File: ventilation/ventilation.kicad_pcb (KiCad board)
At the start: 2 copper layers, 36.8 x 27 mm, 34 parts, among them J1 Conn_01x03_Pin, J2 Conn_01x04_Pin, J3 Conn_01x04_Pin, J7 Conn_01x02_Pin, Q1 IRLML6402, Q2 BC847, U1 STM32L051C8Tx, U2 MCP1700x-330xxTT

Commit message: New version
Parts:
- added H1: MountingHole, MountingHole:MountingHole_2.5mm, F.Cu at (191.4, 79.2)
- added H2: MountingHole, MountingHole:MountingHole_2.5mm, F.Cu at (191.4, 97.8)
- moved NRF1 8.91 mm to (183.9, 84.1), turned to 0 degrees
- moved C8 7.23 mm to (184.0, 84.9), turned to -90 degrees
- moved C7 5.85 mm to (186.6, 84.9), turned to -90 degrees
- moved R7 5.56 mm to (172.4, 100.0)
- moved C4 5.35 mm to (176.1, 91.2)
- moved C10 5.20 mm to (167.8, 87.3), turned to 90 degrees
- moved R9 4.63 mm to (166.0, 78.1), turned to -90 degrees
- moved C5 4.15 mm to (181.4, 84.9)
- moved C2 3.67 mm to (174.4, 84.9), turned to -90 degrees
- moved R3 3.64 mm to (168.8, 95.8), turned to 180 degrees
- moved R6 3.28 mm to (178.8, 98.2), turned to 180 degrees
- moved R10 2.77 mm to (166.7, 81.3), turned to 0 degrees
- moved C6 2.72 mm to (172.3, 97.8), turned to 0 degrees
- moved C9 2.57 mm to (177.7, 97.9), turned to 180 degrees
- moved R8 2.57 mm to (177.7, 100.1), turned to 180 degrees
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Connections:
- J1 pad 2: /VCC_SERVO -> /SIG_SERVO
- J1 pad 3: /SIG_SERVO -> /VCC_SERVO
- J2 pad 3: /I2C_SDA -> /I2C_SCL
- J2 pad 4: /I2C_SCL -> /I2C_SDA
- U1 pad 12: unconnected-(U1-PA2-Pad12) -> /SW_SERVO
- U1 pad 13: /SPI_CE -> unconnected-(U1-PA3-Pad13)
- U1 pad 14: /SPI_CSN -> unconnected-(U1-PA4-Pad14)
- U1 pad 21: unconnected-(U1-PB10-Pad21) -> /SPI_CSN
- U1 pad 22: unconnected-(U1-PB11-Pad22) -> /SPI_CE
- U1 pad 25: /LED_GREEN -> /LED_RED
- U1 pad 28: /LED_RED -> /LED_GREEN
- U1 pad 6: /SW_SERVO -> unconnected-(U1-PH1-Pad6)
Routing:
- net +3V3: track 0.00 -> 90.0 mm, vias 0 -> 6
- net GND: track 0.00 -> 37.8 mm, vias 0 -> 5
- net /RESET: track 0.00 -> 31.2 mm, vias 0 -> 1
- net /BOOT: track 0.00 -> 27.6 mm
- net +BATT: track 0.00 -> 18.0 mm
- net /I2C_SCL: track 0.00 -> 16.2 mm
- net /I2C_SDA: track 0.00 -> 14.9 mm
- net /SPI_SCK: track 0.00 -> 13.1 mm
- net /G_FET: track 0.00 -> 12.7 mm
- net /VCC_SERVO: track 0.00 -> 12.2 mm
- net /ADC_V_EXT: track 0.00 -> 12.1 mm
- net Net-(U1-PB3): track 0.00 -> 10.9 mm
- net /SWCLK: track 0.00 -> 9.44 mm
- net /LED_GREEN: track 0.00 -> 9.02 mm
- net /USART1_TX: track 0.00 -> 7.75 mm
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- added copper zone on B.Cu, net GND
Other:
- board size 36.8 x 27 mm -> 38 x 27 mm

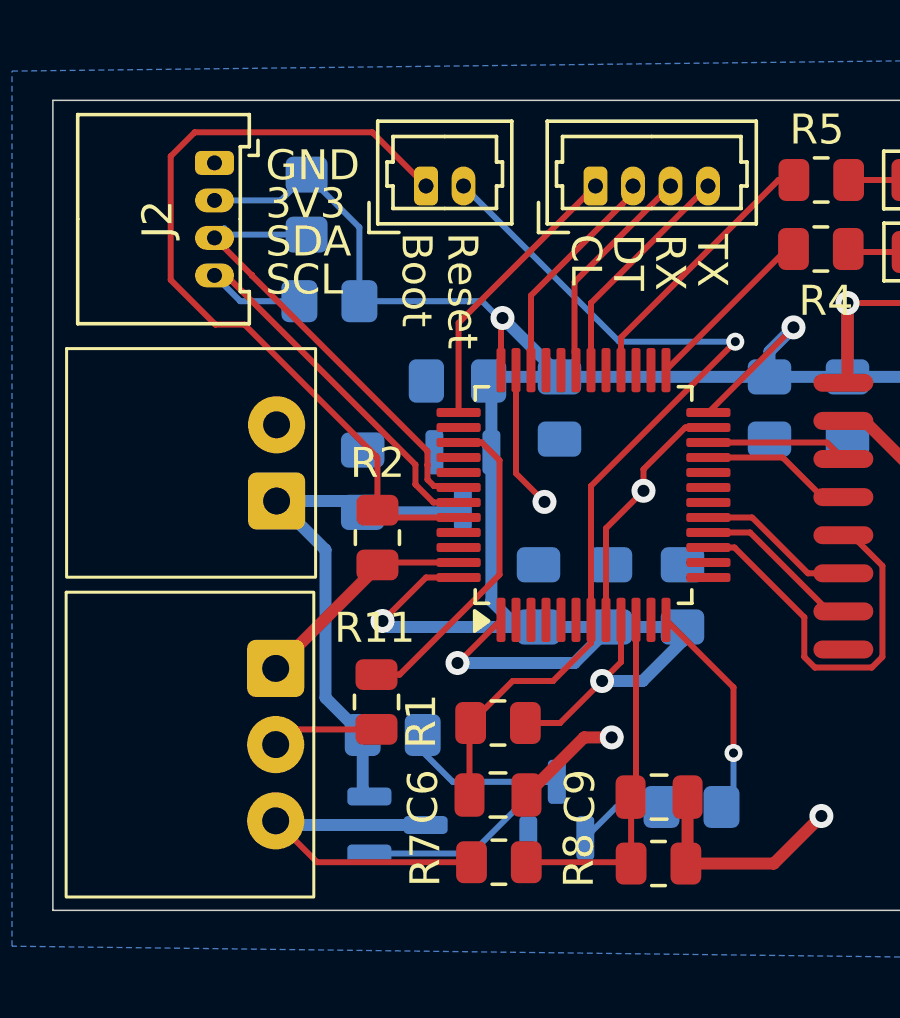
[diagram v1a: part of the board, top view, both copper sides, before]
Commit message: Changed SOT23 footprints to hand solder
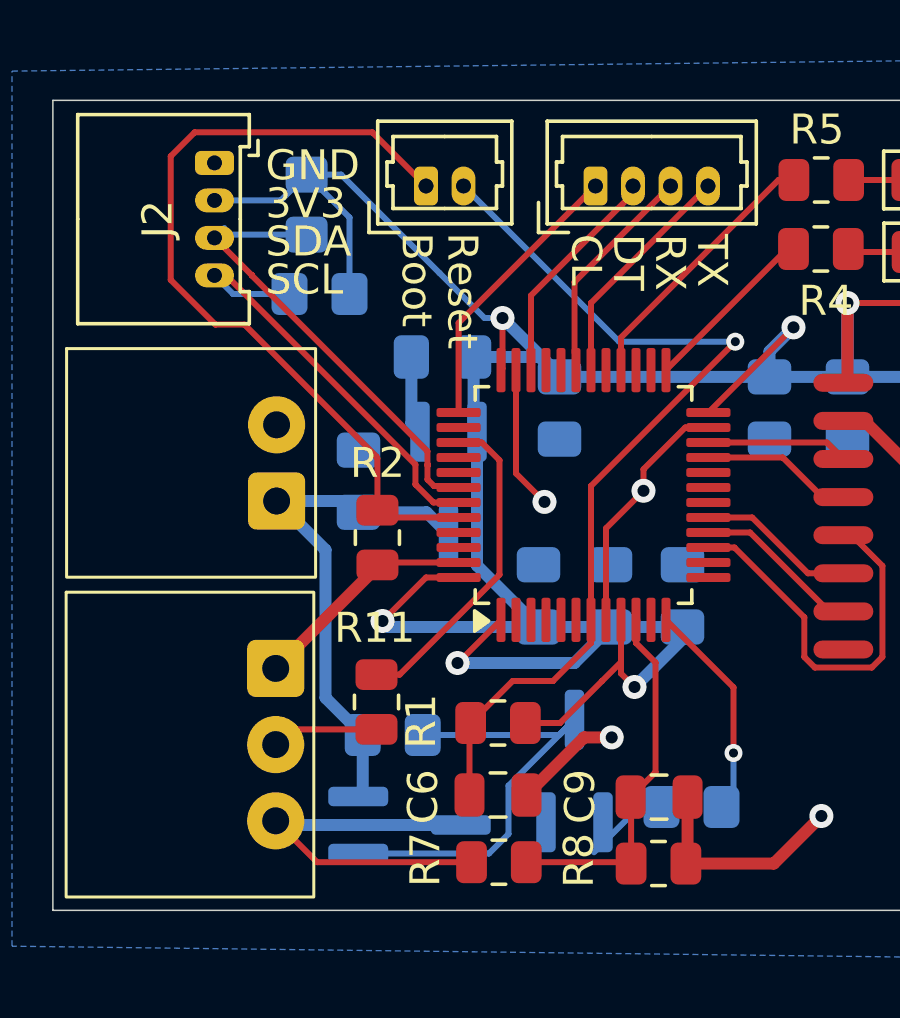
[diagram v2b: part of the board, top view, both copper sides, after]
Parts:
- Q1, Q2, U2: footprint Package_TO_SOT_SMD:SOT-23 -> Package_TO_SOT_SMD:TSOT-23_HandSoldering
- moved Q2 1.43 mm to (174.9, 97.0)
- moved C11 0.94 mm to (170.5, 83.2)
- moved U2 0.49 mm to (170.7, 87.4)
- moved R10 0.41 mm to (166.4, 81.1)
- moved Q1 0.40 mm to (169.4, 98.8)
- moved C10 0.14 mm to (167.7, 87.3)
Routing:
- net +3V3: track 90.0 -> 96.5 mm
- net /G_FET: track 12.7 -> 15.8 mm
- net GND: track 37.8 -> 40.4 mm
- net /VCC_SERVO: track 12.2 -> 13.3 mm

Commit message: New version
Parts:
- added J4: Conn_01x04_Pin, PVDW_custom:Molex_PicoBlade_1x04_P1.25mm_Vertical, F.Cu at (185.7, 98.2)
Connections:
- U1 pad 13: unconnected-(U1-PA3-Pad13) -> /PA3
- U1 pad 14: unconnected-(U1-PA4-Pad14) -> /PA4
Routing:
- net /PA4: track 0.00 -> 11.3 mm
- net /PA3: track 0.00 -> 9.79 mm
- net +3V3: track 96.5 -> 104.5 mm
- net GND: track 40.4 -> 39.3 mm, vias 5 -> 4

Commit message: New version
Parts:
- removed C5: 100n, Capacitor_SMD:C_0805_2012Metric_Pad1.18x1.45mm_HandSolder
- removed J1: Conn_01x03_Pin, PVDW_custom:Connector_1x3_p2.54_hortizontal
- removed J4: Conn_01x04_Pin, PVDW_custom:Molex_PicoBlade_1x04_P1.25mm_Vertical
- removed J5: ~, PVDW_custom:Connector_1x2_p2.54_horizontal
- removed J7: Conn_01x02_Pin, PVDW_custom:Molex_PicoBlade_P1.25mm_Vertical
- added J6: Conn_01x10_Pin, PVDW_custom:FFC_1x10_P1.00mm_Horizontal, F.Cu at (177.2, 80.1)
- J2: footprint PVDW_custom:Molex_PicoBlade_53048-0410_1x04_P1.25mm_Horizontal -> PVDW_custom:Connector_1x4_p2.54_hortizontal
- J3: footprint PVDW_custom:Molex_PicoBlade_1x04_P1.25mm_Vertical -> PVDW_custom:Connector_1x4_p2.54_hortizontal
- moved J3 23.6 mm to (164.8, 98.5)
- moved R4 20.5 mm to (182.0, 100.0)
- moved D2 20.4 mm to (186.8, 97.7)
- moved R5 20.4 mm to (182.0, 97.7)
- moved D1 20.4 mm to (186.8, 100.1)
- moved R11 10.0 mm to (167.7, 84.7), turned to -90 degrees
- moved J2 8.97 mm to (164.8, 85.5), turned to 0 degrees
- moved C4 7.26 mm to (179.4, 84.7), turned to -90 degrees
- moved R9 6.56 mm to (172.3, 76.5), turned to 180 degrees
- moved R10 6.40 mm to (172.3, 78.7)
- moved C10 5.46 mm to (168.3, 92.8)
- moved R6 4.81 mm to (177.8, 93.5)
- moved C3 4.62 mm to (177.8, 89.1), turned to 0 degrees
- moved R1 4.57 mm to (168.0, 96.8), turned to -90 degrees
- moved R3 4.24 mm to (172.4, 93.5), turned to 0 degrees
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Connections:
- J3 pad 1: /SWCLK -> GND
- J3 pad 2: /SWDIO -> +BATT
- J3 pad 3: /USART1_RX -> /SIG_SERVO
- J3 pad 4: /USART1_TX -> /VCC_SERVO
- U1 pad 11: unconnected-(U1-PA1-Pad11) -> /LED_RED
- U1 pad 12: /SW_SERVO -> /LED_GREEN
- U1 pad 13: /PA3 -> /SW_SERVO
- U1 pad 14: /PA4 -> unconnected-(U1-PA4-Pad14)
- U1 pad 25: /LED_RED -> unconnected-(U1-PB12-Pad25)
- U1 pad 27: unconnected-(U1-PB14-Pad27) -> /PB14
- U1 pad 28: /LED_GREEN -> /PB15
- U1 pad 42: /I2C_SCL -> unconnected-(U1-PB6-Pad42)
- U1 pad 43: /I2C_SDA -> unconnected-(U1-PB7-Pad43)
- U1 pad 45: unconnected-(U1-PB8-Pad45) -> /I2C_SCL
- U1 pad 46: unconnected-(U1-PB9-Pad46) -> /I2C_SDA
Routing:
- net /SIG_SERVO: track 3.57 -> 19.5 mm, vias 0 -> 1
- net /PA4: track 11.3 -> 0.00 mm
- net GND: track 39.3 -> 29.4 mm, vias 4 -> 8
- net /PA3: track 9.79 -> 0.00 mm
- net /BOOT: track 27.6 -> 19.0 mm
- net /RESET: track 31.2 -> 38.0 mm, vias 1 -> 0
- net Net-(U1-PB3): track 10.9 -> 4.35 mm
- net /I2C_SCL: track 16.2 -> 21.8 mm
- net /I2C_SDA: track 14.6 -> 20.1 mm
- net /PB14: track 0.00 -> 5.30 mm
- net /PB15: track 0.00 -> 5.10 mm
- net /G_FET: track 15.8 -> 11.0 mm
- net /LED_GREEN: track 9.02 -> 5.41 mm
- net +3V3: track 104.5 -> 107.6 mm
- net /SW_SERVO: track 7.34 -> 4.52 mm
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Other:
- board size 38 x 27 mm -> 38 x 28.7 mm

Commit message: New versions
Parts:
- removed J6: Conn_01x10_Pin, PVDW_custom:FFC_1x10_P1.00mm_Horizontal
- added J1: Conn_01x10_Pin, Connector_PinHeader_2.54mm:PinHeader_2x05_P2.54mm_Vertical, F.Cu at (186.8, 75.9)
- Q1, Q2, U2: footprint Package_TO_SOT_SMD:TSOT-23_HandSoldering -> Package_TO_SOT_SMD:SOT-23
- moved R9 4.37 mm to (168.9, 79.2)
- moved R10 3.83 mm to (168.9, 77.0)
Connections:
- J2 pad 1: GND -> +3V3
- J2 pad 2: +3V3 -> GND
- J2 pad 3: /I2C_SCL -> /I2C_SDA
- J2 pad 4: /I2C_SDA -> /I2C_SCL
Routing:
- net /PB15: track 5.10 -> 13.2 mm
- net /USART1_RX: track 4.89 -> 12.3 mm
- net /SWCLK: track 8.22 -> 15.4 mm
- net /RESET: track 38.0 -> 44.8 mm
- net /PB14: track 5.30 -> 10.3 mm
- net /USART1_TX: track 5.10 -> 9.71 mm
- net /SWDIO: track 5.10 -> 9.01 mm
- net /BOOT: track 19.0 -> 22.6 mm
- net /I2C_SCL: track 21.8 -> 18.2 mm
- net GND: track 29.4 -> 26.3 mm, vias 8 -> 7
- net /G_FET: track 11.0 -> 13.8 mm, vias 0 -> 2
- net +3V3: track 107.6 -> 105.7 mm
- net /I2C_SDA: track 20.1 -> 21.4 mm

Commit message: Order versions
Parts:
- removed J1: Conn_01x10_Pin, Connector_PinHeader_2.54mm:PinHeader_2x05_P2.54mm_Vertical
- added Boot1: TestPoint, TestPoint:TestPoint_Pad_2.0x2.0mm, F.Cu at (167.8, 86.1)
- added J4: Conn_01x08_Pin, Connector_PinHeader_2.54mm:PinHeader_2x04_P2.54mm_Vertical, F.Cu at (176.0, 78.4)
- added Reset1: TestPoint, TestPoint:TestPoint_Pad_2.0x2.0mm, F.Cu at (168.6, 96.4)
- moved R1 4.41 mm to (172.4, 96.3), turned to 180 degrees
- moved R11 2.71 mm to (168.5, 82.1), turned to 0 degrees
- moved C6 0.67 mm to (172.4, 98.3)
- moved R2 0.54 mm to (168.2, 88.6), turned to 180 degrees
- moved R7 0.36 mm to (172.4, 100.4)
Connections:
- net Net-(U1-PB3) renamed /SIG_SERVO_OUT
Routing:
- net /RESET: track 44.8 -> 10.8 mm
- net /BOOT: track 22.6 -> 6.18 mm
- net /PB14: track 10.3 -> 16.3 mm
- net /SWCLK: track 15.4 -> 10.1 mm
- net /PB15: track 13.2 -> 17.2 mm
- net /USART1_RX: track 12.3 -> 9.73 mm
- net GND: track 26.3 -> 23.9 mm, vias 7 -> 8
- net /SIG_SERVO_OUT: track 4.35 -> 6.66 mm
- net +3V3: track 105.7 -> 107.8 mm, vias 6 -> 7
- net /USART1_TX: track 9.71 -> 11.2 mm
- net /SIG_SERVO: track 19.5 -> 18.9 mm, vias 1 -> 0

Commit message: New order
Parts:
- removed Boot1, Reset1: TestPoint, TestPoint:TestPoint_Pad_2.0x2.0mm
- removed J3: Conn_01x04_Pin, PVDW_custom:Connector_1x4_p2.54_hortizontal
- added BOOT1: SW_Push, PVDW_custom:SW_Push_4Pin, B.Cu at (166.2, 84.9)
- added C12: 10n, Capacitor_SMD:C_0805_2012Metric, F.Cu at (170.3, 102.6)
- added J1: Conn_01x02_Pin, PVDW_custom:Connector_1x2_p2.54_horizontal, F.Cu at (161.3, 90.9)
- added J5: Conn_01x03_Pin, PVDW_custom:Connector_1x3_p2.54_hortizontal, F.Cu at (161.3, 101.8)
- added Q3: IRLML6402, Package_TO_SOT_SMD:SOT-23, F.Cu at (175.1, 101.6)
- added R15: 0.1, Resistor_SMD:R_2512_6332Metric_Pad1.40x3.35mm_HandSolder, F.Cu at (165.8, 99.5)
- added R16: 10k, Resistor_SMD:R_0805_2012Metric_Pad1.20x1.40mm_HandSolder, F.Cu at (175.2, 98.4)
- added RESET1: SW_Push, PVDW_custom:SW_Push_4Pin, B.Cu at (169.3, 99.4)
- added U3: INA180A1, Package_TO_SOT_SMD:SOT-23-5, F.Cu at (170.3, 99.2)
- C6: value 100n -> 10n; moved to B.Cu
- J4: footprint Connector_PinHeader_2.54mm:PinHeader_2x04_P2.54mm_Vertical -> Connector_PinHeader_2.54mm:PinHeader_1x08_P2.54mm_Vertical
- Q1, Q2: moved to F.Cu
- R1: value 100k -> 10k; moved to B.Cu
- R3: value 40k -> 43k; moved to F.Cu
- R4: value 10k -> 1k2
- R5: value 10k -> 820
- R6: value 40k -> 43k; footprint Resistor_SMD:R_0805_2012Metric_Pad1.20x1.40mm_HandSolder -> Resistor_SMD:R_0805_2012Metric; moved to F.Cu
- R7: value 3k -> 3k3
- U2: footprint Package_TO_SOT_SMD:SOT-23 -> Package_TO_SOT_SMD:SOT-23_Handsoldering
- moved J4 10.3 mm to (166.5, 74.6)
- moved Q2 9.00 mm to (170.5, 92.5), turned to 180 degrees
- moved R8 8.29 mm to (177.1, 91.8)
- moved Q1 8.14 mm to (165.7, 92.8)
- moved R3 7.86 mm to (165.8, 89.2), turned to 180 degrees
- moved R2 7.76 mm to (165.1, 81.5), turned to 90 degrees
- moved R1 7.08 mm to (175.2, 89.8), turned to -90 degrees
- moved C3 6.60 mm to (172.3, 85.5), turned to 90 degrees
- moved C1 6.33 mm to (175.2, 85.5), turned to 90 degrees
- moved R11 6.30 mm to (164.8, 87.2)
- moved C11 6.23 mm to (170.3, 89.7)
- moved U1 5.41 mm to (173.4, 84.3)
- moved U2 5.41 mm to (170.3, 93.7)
- moved C4 5.34 mm to (175.2, 81.4)
- moved C6 5.17 mm to (175.3, 94.1), turned to -90 degrees
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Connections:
- net /VCC_SERVO renamed /SHUNT_P
- net Net-(D1-K) renamed /LED_RED_R
- net Net-(D2-K) renamed /LED_GREEN_R
- J2 pad 1: +3V3 -> /I2C_SCL
- J2 pad 2: GND -> /I2C_SDA
- J2 pad 3: /I2C_SDA -> GND
- J2 pad 4: /I2C_SCL -> +3V3
- J4 pad 1: /SWCLK -> GND
- J4 pad 3: /SWDIO -> /SWCLK
- J4 pad 4: GND -> /SWDIO
- J4 pad 6: /PB15 -> /USART1_TX
- J4 pad 7: /USART1_TX -> /PB15
- U1 pad 13: /SW_SERVO -> /INA_OUT
- U1 pad 14: unconnected-(U1-PA4-Pad14) -> /SW_I_SERVO
- U1 pad 2: unconnected-(U1-PC13-Pad2) -> /SW_SERVO
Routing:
- net +3V3: track 107.8 -> 129.4 mm, vias 7 -> 8
- net /INA_OUT: track 0.00 -> 18.4 mm
- net /SW_I_SERVO: track 0.00 -> 17.9 mm
- net /LED_RED: track 8.00 -> 18.7 mm, vias 0 -> 2
- net /SHUNT_N: track 0.00 -> 9.24 mm
- net /G_FET: track 13.9 -> 5.88 mm, vias 2 -> 0
- net /PB15: track 17.2 -> 10.4 mm
- net /LED_GREEN: track 5.41 -> 11.6 mm, vias 0 -> 2
- net /INA_VCC: track 0.00 -> 6.10 mm
- net GND: track 23.9 -> 29.4 mm, vias 8 -> 11
- net /SHUNT_P: track 15.7 -> 10.8 mm
- net /PB14: track 16.3 -> 11.9 mm
- net /SPI_MOSI: track 4.45 -> 7.83 mm
- net /SPI_MISO: track 4.77 -> 8.15 mm
- net /I2C_SDA: track 21.4 -> 18.1 mm
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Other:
- board size 38 x 28.7 mm -> 42 x 33 mm
- board text added: "3V3"
- board text added: "B14"
- board text added: "B15"
- board text added: "BAT+"
- board text added: "BAT-"
- board text added: "CLK"
- board text added: "DIO"
- board text added: "GND"
- board text added: "PVDW 2025"
- board text added: "RX"
- board text added: "SCL"
- board text added: "SDA"
- board text added: "SIG"
- board text added: "TX"
- board text added: "VCC"
